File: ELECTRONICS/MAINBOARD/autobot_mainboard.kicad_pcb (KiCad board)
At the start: 4 copper layers, 50 x 38.5 mm, 162 parts, among them IC1 DW3210, J1 USB_C_Receptacle_USB2.0_16P, J10 Conn_01x05_Socket, J12 Conn_01x02_Pin, J17 Conn_01x02_Pin, J18 Conn_01x02_Pin, J19 Conn_02x05_Odd_Even, J20 Conn_02x05_Odd_Even, J4 Conn_01x02_Socket, J7 Conn_01x03_Pin, J8 Conn_Coaxial, J9 Conn_Coaxial, Q1 DMG1012T, Q2 DMG1012T, Q3 DMG1012T, Q4 DMG1012T, Q5 DMG1012T, SW1 RESET, SW2 BOOT, U1 TVS1400DRV, U10 VL53L1X, U11 VL53L1X, U12 VL53L1X, U13 BMI270, U14 BMI270, U16 LP5907MFX-3.3, U18 LP5907MFX-3.3, U19 STM32H743VITx, U2 LMR51430XDDCR, U23 LP5907MFX-3.3, U3 LP5907MFX-3.3, U4 TPD2EUSB30A, U7 STM32G031C_4-6-8_Tx, U8 TVS1400DRV, U9 VL53L1X, Y1 TXC 8Y38472012, Y2 25mhz placeholder

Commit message: functionally finished driver board
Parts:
- removed U8: TVS1400DRV, Package_SON:WSON-6-1EP_2x2mm_P0.65mm_EP1x1.6mm
- added C78: 100n, Capacitor_SMD:C_0402_1005Metric, F.Cu at (35.9, 31.2)
- added D13: PTVS17VZ1USK, Diode_SMD:Nexperia_CFP3_SOD-123W, F.Cu at (30.1, 53.9)
- added J11: Conn_01x01_Socket, Connector_Wire:SolderWire-0.25sqmm_1x01_D0.65mm_OD1.7mm, F.Cu at (60.4, 40.0)
- added J13: Conn_01x01_Socket, Connector_Wire:SolderWire-0.25sqmm_1x01_D0.65mm_OD1.7mm, F.Cu at (13.7, 34.1)
- added J2: Conn_01x01_Socket, Connector_Wire:SolderWire-0.25sqmm_1x01_D0.65mm_OD1.7mm, F.Cu at (60.4, 34.2)
- added J3: Conn_01x01_Socket, Connector_Wire:SolderWire-0.25sqmm_1x01_D0.65mm_OD1.7mm, F.Cu at (13.7, 39.9)
- added J5: Conn_01x01_Socket, Connector_Wire:SolderWire-0.25sqmm_1x01_D0.65mm_OD1.7mm, F.Cu at (60.4, 37.0)
- added J6: Conn_01x01_Socket, Connector_Wire:SolderWire-0.25sqmm_1x01_D0.65mm_OD1.7mm, F.Cu at (13.7, 37.0)
- added SW3: SW_Push, MyFootprintLibrary:SW-SMD_L3.9-W3.0-P4.45, F.Cu at (43.6, 20.1)
- SW1, SW2: footprint Button_Switch_THT:SW_PUSH_6mm -> MyFootprintLibrary:SW-SMD_L3.9-W3.0-P4.45
- moved SW1 56.8 mm to (283.6, 41.2)
- moved SW2 54.1 mm to (283.6, 45.5)
- moved U19 24.0 mm to (257.6, 57.2)
- moved C36 1.23 mm to (37.1, 29.8)
- moved C37 1.10 mm to (37.1, 28.9)
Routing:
- net /STM32G0/nRESET: track 0.00 -> 18.2 mm, vias 0 -> 2
- net GNDREF: track 48.1 -> 51.9 mm, vias 22 -> 26
- net +3V3: track 54.1 -> 56.1 mm
- net +24V: track 7.77 -> 9.68 mm
- net Net-(J3-Pin_1): track 6.92 -> 7.91 mm
- net Net-(J13-Pin_1): track 6.92 -> 7.87 mm
- net Net-(J11-Pin_1): track 7.05 -> 7.81 mm
- net Net-(J2-Pin_1): track 7.22 -> 7.81 mm

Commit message: driver done, unpolished
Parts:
- removed C1: 1u, Capacitor_SMD:C_0603_1608Metric
- removed C19, C21, C23, C25, C27, C28, C29, C30, C40, C45, C46, C47, C57, C60, C62, C63, C64, C65, C66, C67, C68, C69, C70, C71, C72: 100n, Capacitor_SMD:C_0402_1005Metric
- removed C2, C3: 100n, Capacitor_SMD:C_0603_1608Metric
- removed C20, C22, C24, C26, C49, C50: 10u, Capacitor_SMD:C_0402_1005Metric
- removed C34, C35, C5, C53, C54, C6, C61: 1u, Capacitor_SMD:C_0402_1005Metric
- removed C38, C39: 2p, Capacitor_SMD:C_0402_1005Metric
- removed C4: 47u, Capacitor_SMD:C_0603_1608Metric
- removed C41, C42, C43: 4.7n, Capacitor_SMD:C_0402_1005Metric
- removed C44: 220n, Capacitor_SMD:C_0402_1005Metric
- removed C48: 4.7u, Capacitor_SMD:C_0402_1005Metric
- removed C51, C52, C55, C56: 12p, Capacitor_SMD:C_0402_1005Metric
- removed C58, C59: 2.2u, Capacitor_SMD:C_0402_1005Metric
- removed C73: 4u7, Capacitor_SMD:C_0402_1005Metric
- removed D1: SS24, Diode_SMD:D_SMA
- removed D2, D3, D4: LED, LED_SMD:LED_0402_1005Metric
- removed FB2: fb, Resistor_SMD:R_0603_1608Metric
- removed FB3: FerriteBead_Small, Resistor_SMD:R_0402_1005Metric
- removed IC1: DW3210, MyFootprintLibrary:qfn_DW3220_QOR-M
- removed J1: USB_C_Receptacle_USB2.0_16P, Connector_USB:USB_C_Receptacle_GCT_USB4105-xx-A_16P_TopMnt_Horizontal
- removed J10: Conn_01x05_Socket, Connector_PinHeader_2.54mm:PinHeader_1x05_P2.54mm_Vertical
- removed J12: Conn_01x02_Pin, Connector_PinSocket_2.54mm:PinSocket_1x02_P2.54mm_Vertical
- removed J19: Conn_02x05_Odd_Even, Connector_PinSocket_2.54mm:PinSocket_2x05_P2.54mm_Vertical
- removed J7: Conn_01x03_Pin, Connector_PinHeader_2.54mm:PinHeader_1x03_P2.54mm_Vertical
- removed J8, J9: Conn_Coaxial, Connector_Coaxial:U.FL_Hirose_U.FL-R-SMT-1_Vertical
- removed L1: 5.6u, Inductor_SMD:L_APV_APH0840
- removed Q1, Q2, Q3: DMG1012T, Package_TO_SOT_SMD:SOT-523
- removed R1: 162k, Resistor_SMD:R_0603_1608Metric
- removed R15, R16, R21: 10k, Resistor_SMD:R_0402_1005Metric
- removed R17: 100K, Resistor_SMD:R_0402_1005Metric
- removed R18, R19, R20: R, Resistor_SMD:R_0402_1005Metric
- removed R2: 22.1k, Resistor_SMD:R_0603_1608Metric
- removed R22: 47, Resistor_SMD:R_0402_1005Metric_Pad0.72x0.64mm_HandSolder
- removed R3, R4: 5.1k, Resistor_SMD:R_0402_1005Metric
- removed R5, R6: 22, Resistor_SMD:R_0402_1005Metric
- removed SW1: RESET, MyFootprintLibrary:SW-SMD_L3.9-W3.0-P4.45
- removed SW2: BOOT, MyFootprintLibrary:SW-SMD_L3.9-W3.0-P4.45
- removed U1: TVS1400DRV, Package_SON:WSON-6-1EP_2x2mm_P0.65mm_EP1x1.6mm
- removed U10, U11, U12, U9: VL53L1X, Connector_JST:JST_PH_S6B-PH-K_1x06_P2.00mm_Horizontal
- removed U13, U14: BMI270, MyFootprintLibrary:BMI270_BOS-M
- removed U16, U18, U3: LP5907MFX-3.3, Package_TO_SOT_SMD:SOT-23-5
- removed U19: STM32H743VITx, Package_QFP:LQFP-100_14x14mm_P0.5mm
- removed U2: LMR51430XDDCR, MyFootprintLibrary:SOT-23-THIN-6_DDC_TEX
- removed U4: TPD2EUSB30A, Package_TO_SOT_SMD:Texas_DRT-3
- removed Y1: TXC 8Y38472012, Crystal:Crystal_SMD_2016-4Pin_2.0x1.6mm
- removed Y2: 25mhz placeholder, Crystal:Crystal_SMD_2016-4Pin_2.0x1.6mm
- U5, U6: footprint MyFootprintLibrary:VQFN-40_L7.0-W5.0-P0.50-BL-EP5.7 -> MyFootprintLibrary:VQFN40_RGF_TEX_mct8316
- moved C12 0.23 mm to (45.5, 40.5)
- moved C74 0.23 mm to (28.6, 33.5)
- turned U5 to 90 degrees
- turned U6 to -90 degrees
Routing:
- net +5V: track 81.4 -> 71.2 mm
- net GNDREF: track 51.9 -> 41.7 mm, vias 26 -> 29
- net /STM32G0/nRESET: track 18.2 -> 17.7 mm

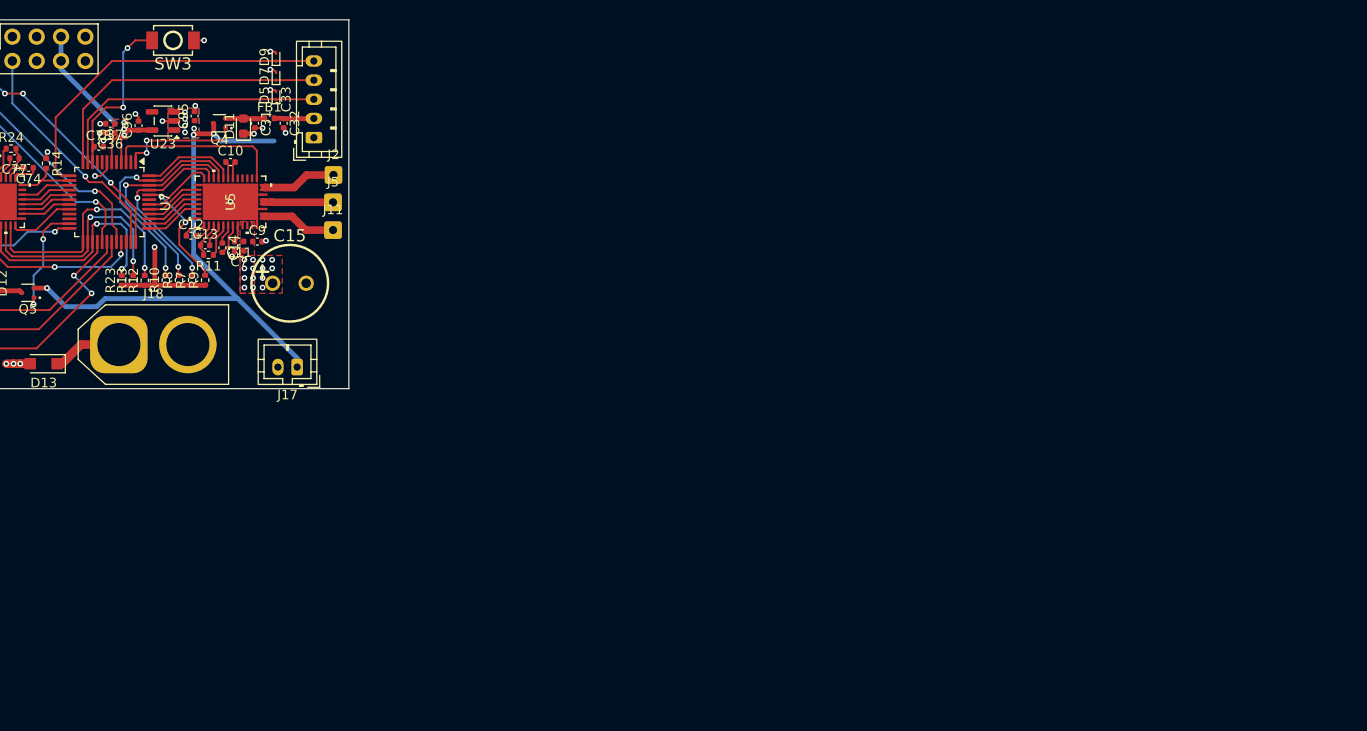
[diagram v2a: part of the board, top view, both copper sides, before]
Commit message: edit boost converter, added gnd planes, polish later
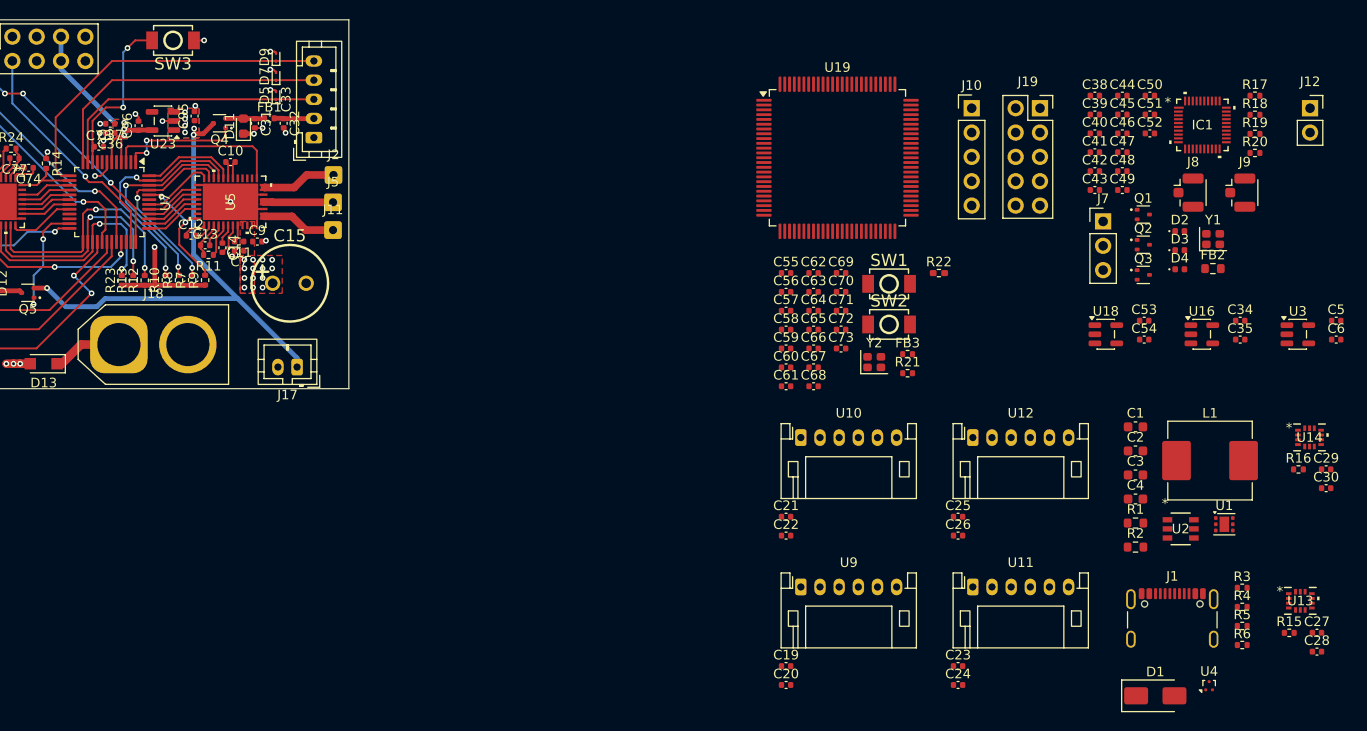
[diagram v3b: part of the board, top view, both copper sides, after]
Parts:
- added C1: 1u, Capacitor_SMD:C_0603_1608Metric, F.Cu at (144.1, 60.5)
- added C19: 100n, Capacitor_SMD:C_0402_1005Metric, F.Cu at (107.6, 85.5)
- added C2: 100n, Capacitor_SMD:C_0603_1608Metric, F.Cu at (144.1, 63.0)
- added C20: 10u, Capacitor_SMD:C_0402_1005Metric, F.Cu at (107.6, 87.4)
- added C21: 100n, Capacitor_SMD:C_0402_1005Metric, F.Cu at (107.6, 69.9)
- added C22: 10u, Capacitor_SMD:C_0402_1005Metric, F.Cu at (107.6, 71.8)
- added C23: 100n, Capacitor_SMD:C_0402_1005Metric, F.Cu at (125.6, 85.5)
- added C24: 10u, Capacitor_SMD:C_0402_1005Metric, F.Cu at (125.6, 87.4)
- added C25: 100n, Capacitor_SMD:C_0402_1005Metric, F.Cu at (125.6, 69.9)
- added C26: 10u, Capacitor_SMD:C_0402_1005Metric, F.Cu at (125.6, 71.8)
- added C27: 100n, Capacitor_SMD:C_0402_1005Metric, F.Cu at (163.1, 82.0)
- added C28: 100n, Capacitor_SMD:C_0402_1005Metric, F.Cu at (163.1, 84.0)
- added C29: 100n, Capacitor_SMD:C_0402_1005Metric, F.Cu at (164.0, 64.9)
- added C3: 100n, Capacitor_SMD:C_0603_1608Metric, F.Cu at (144.1, 65.5)
- added C30: 100n, Capacitor_SMD:C_0402_1005Metric, F.Cu at (164.0, 66.9)
- added C34: 1u, Capacitor_SMD:C_0402_1005Metric, F.Cu at (155.0, 49.4)
- added C35: 1u, Capacitor_SMD:C_0402_1005Metric, F.Cu at (155.0, 51.4)
- added C38: 2p, Capacitor_SMD:C_0402_1005Metric, F.Cu at (139.9, 25.9)
- added C39: 2p, Capacitor_SMD:C_0402_1005Metric, F.Cu at (139.9, 27.9)
- added C4: 47u, Capacitor_SMD:C_0603_1608Metric, F.Cu at (144.1, 68.0)
- added C40: 100n, Capacitor_SMD:C_0402_1005Metric, F.Cu at (139.9, 29.9)
- added C41: 4.7n, Capacitor_SMD:C_0402_1005Metric, F.Cu at (139.9, 31.8)
- added C42: 4.7n, Capacitor_SMD:C_0402_1005Metric, F.Cu at (139.9, 33.8)
- added C43: 4.7n, Capacitor_SMD:C_0402_1005Metric, F.Cu at (139.9, 35.8)
- added C44: 220n, Capacitor_SMD:C_0402_1005Metric, F.Cu at (142.7, 25.9)
- added C45: 100n, Capacitor_SMD:C_0402_1005Metric, F.Cu at (142.7, 27.9)
- added C46: 100n, Capacitor_SMD:C_0402_1005Metric, F.Cu at (142.7, 29.9)
- added C47: 100n, Capacitor_SMD:C_0402_1005Metric, F.Cu at (142.7, 31.8)
- added C48: 4.7u, Capacitor_SMD:C_0402_1005Metric, F.Cu at (142.7, 33.8)
- added C49: 10u, Capacitor_SMD:C_0402_1005Metric, F.Cu at (142.7, 35.8)
- added C5: 1u, Capacitor_SMD:C_0402_1005Metric, F.Cu at (165.1, 49.4)
- added C50: 10u, Capacitor_SMD:C_0402_1005Metric, F.Cu at (145.6, 25.9)
- added C51: 12p, Capacitor_SMD:C_0402_1005Metric, F.Cu at (145.6, 27.9)
- added C52: 12p, Capacitor_SMD:C_0402_1005Metric, F.Cu at (145.6, 29.9)
- added C53: 1u, Capacitor_SMD:C_0402_1005Metric, F.Cu at (145.0, 49.4)
- added C54: 1u, Capacitor_SMD:C_0402_1005Metric, F.Cu at (145.0, 51.4)
- added C55: 12p, Capacitor_SMD:C_0402_1005Metric, F.Cu at (107.6, 44.4)
- added C56: 12p, Capacitor_SMD:C_0402_1005Metric, F.Cu at (107.6, 46.4)
- added C57: 100n, Capacitor_SMD:C_0402_1005Metric, F.Cu at (107.6, 48.4)
- added C58: 2.2u, Capacitor_SMD:C_0402_1005Metric, F.Cu at (107.6, 50.3)
- added C59: 2.2u, Capacitor_SMD:C_0402_1005Metric, F.Cu at (107.6, 52.3)
- added C6: 1u, Capacitor_SMD:C_0402_1005Metric, F.Cu at (165.1, 51.4)
- added C60: 100n, Capacitor_SMD:C_0402_1005Metric, F.Cu at (107.6, 54.3)
- added C61: 1u, Capacitor_SMD:C_0402_1005Metric, F.Cu at (107.6, 56.2)
- added C62: 100n, Capacitor_SMD:C_0402_1005Metric, F.Cu at (110.5, 44.4)
- added C63: 100n, Capacitor_SMD:C_0402_1005Metric, F.Cu at (110.5, 46.4)
- added C64: 100n, Capacitor_SMD:C_0402_1005Metric, F.Cu at (110.5, 48.4)
- added C65: 100n, Capacitor_SMD:C_0402_1005Metric, F.Cu at (110.5, 50.3)
- added C66: 100n, Capacitor_SMD:C_0402_1005Metric, F.Cu at (110.5, 52.3)
- added C67: 100n, Capacitor_SMD:C_0402_1005Metric, F.Cu at (110.5, 54.3)
- added C68: 100n, Capacitor_SMD:C_0402_1005Metric, F.Cu at (110.5, 56.2)
- added C69: 100n, Capacitor_SMD:C_0402_1005Metric, F.Cu at (113.4, 44.4)
- added C70: 100n, Capacitor_SMD:C_0402_1005Metric, F.Cu at (113.4, 46.4)
- added C71: 100n, Capacitor_SMD:C_0402_1005Metric, F.Cu at (113.4, 48.4)
- added C72: 100n, Capacitor_SMD:C_0402_1005Metric, F.Cu at (113.4, 50.3)
- added C73: 4u7, Capacitor_SMD:C_0402_1005Metric, F.Cu at (113.4, 52.3)
- added D1: SS24, Diode_SMD:D_SMA, F.Cu at (146.2, 88.6)
- added D2: LED, LED_SMD:LED_0402_1005Metric, F.Cu at (148.7, 40.1)
- added D3: LED, LED_SMD:LED_0402_1005Metric, F.Cu at (148.7, 42.0)
- added D4: LED, LED_SMD:LED_0402_1005Metric, F.Cu at (148.7, 44.0)
- added FB2: fb, Resistor_SMD:R_0603_1608Metric, F.Cu at (152.2, 44.0)
- added FB3: FerriteBead_Small, Resistor_SMD:R_0402_1005Metric, F.Cu at (120.3, 52.9)
- added IC1: DW3210, MyFootprintLibrary:qfn_DW3220_QOR-M, F.Cu at (151.1, 29.0)
- added J1: USB_C_Receptacle_USB2.0_16P, Connector_USB:USB_C_Receptacle_GCT_USB4105-xx-A_16P_TopMnt_Horizontal, F.Cu at (147.9, 81.6)
- added J10: Conn_01x05_Socket, Connector_PinHeader_2.54mm:PinHeader_1x05_P2.54mm_Vertical, F.Cu at (127.0, 27.2)
- added J12: Conn_01x02_Pin, Connector_PinSocket_2.54mm:PinSocket_1x02_P2.54mm_Vertical, F.Cu at (162.3, 27.2)
- added J19: Conn_02x05_Odd_Even, Connector_PinSocket_2.54mm:PinSocket_2x05_P2.54mm_Vertical, F.Cu at (134.1, 27.2)
- added J7: Conn_01x03_Pin, Connector_PinHeader_2.54mm:PinHeader_1x03_P2.54mm_Vertical, F.Cu at (140.7, 39.0)
- added J8: Conn_Coaxial, Connector_Coaxial:U.FL_Hirose_U.FL-R-SMT-1_Vertical, F.Cu at (150.1, 36.0)
- added J9: Conn_Coaxial, Connector_Coaxial:U.FL_Hirose_U.FL-R-SMT-1_Vertical, F.Cu at (155.5, 36.0)
- added L1: 5.6u, Inductor_SMD:L_APV_APH0840, F.Cu at (151.9, 64.0)
- added Q1: DMG1012T, Package_TO_SOT_SMD:SOT-523, F.Cu at (144.9, 38.3)
- added Q2: DMG1012T, Package_TO_SOT_SMD:SOT-523, F.Cu at (144.9, 41.5)
- added Q3: DMG1012T, Package_TO_SOT_SMD:SOT-523, F.Cu at (144.9, 44.6)
- added R1: 162k, Resistor_SMD:R_0603_1608Metric, F.Cu at (144.1, 70.5)
- added R15: 10k, Resistor_SMD:R_0402_1005Metric, F.Cu at (160.2, 82.0)
- added R16: 10k, Resistor_SMD:R_0402_1005Metric, F.Cu at (161.1, 64.9)
- added R17: 100K, Resistor_SMD:R_0402_1005Metric, F.Cu at (156.6, 25.9)
- added R18: R, Resistor_SMD:R_0402_1005Metric, F.Cu at (156.6, 27.9)
- added R19: R, Resistor_SMD:R_0402_1005Metric, F.Cu at (156.6, 29.9)
- added R2: 22.1k, Resistor_SMD:R_0603_1608Metric, F.Cu at (144.1, 73.0)
- added R20: R, Resistor_SMD:R_0402_1005Metric, F.Cu at (156.6, 31.9)
- added R21: 10k, Resistor_SMD:R_0402_1005Metric, F.Cu at (120.3, 54.9)
- added R22: 47, Resistor_SMD:R_0402_1005Metric_Pad0.72x0.64mm_HandSolder, F.Cu at (123.6, 44.4)
- added R3: 5.1k, Resistor_SMD:R_0402_1005Metric, F.Cu at (155.2, 77.3)
- added R4: 5.1k, Resistor_SMD:R_0402_1005Metric, F.Cu at (155.2, 79.3)
- added R5: 22, Resistor_SMD:R_0402_1005Metric, F.Cu at (155.2, 81.3)
- added R6: 22, Resistor_SMD:R_0402_1005Metric, F.Cu at (155.2, 83.3)
- added SW1: RESET, MyFootprintLibrary:SW-SMD_L3.9-W3.0-P4.45, F.Cu at (118.4, 45.6)
- added SW2: BOOT, MyFootprintLibrary:SW-SMD_L3.9-W3.0-P4.45, F.Cu at (118.4, 49.8)
- added U1: TVS1400DRV, Package_SON:WSON-6-1EP_2x2mm_P0.65mm_EP1x1.6mm, F.Cu at (153.4, 70.7)
- added U10: VL53L1X, Connector_JST:JST_PH_S6B-PH-K_1x06_P2.00mm_Horizontal, F.Cu at (109.2, 61.6)
- added U11: VL53L1X, Connector_JST:JST_PH_S6B-PH-K_1x06_P2.00mm_Horizontal, F.Cu at (127.1, 77.2)
- added U12: VL53L1X, Connector_JST:JST_PH_S6B-PH-K_1x06_P2.00mm_Horizontal, F.Cu at (127.1, 61.6)
- added U13: BMI270, MyFootprintLibrary:BMI270_BOS-M, F.Cu at (161.3, 78.6)
- added U14: BMI270, MyFootprintLibrary:BMI270_BOS-M, F.Cu at (162.3, 61.6)
- added U16: LP5907MFX-3.3, Package_TO_SOT_SMD:SOT-23-5, F.Cu at (151.0, 50.8)
- added U18: LP5907MFX-3.3, Package_TO_SOT_SMD:SOT-23-5, F.Cu at (141.0, 50.8)
- added U19: STM32H743VITx, Package_QFP:LQFP-100_14x14mm_P0.5mm, F.Cu at (113.0, 32.4)
- added U2: LMR51430XDDCR, MyFootprintLibrary:SOT-23-THIN-6_DDC_TEX, F.Cu at (148.8, 71.1)
- added U3: LP5907MFX-3.3, Package_TO_SOT_SMD:SOT-23-5, F.Cu at (161.1, 50.8)
- added U4: TPD2EUSB30A, Package_TO_SOT_SMD:Texas_DRT-3, F.Cu at (151.8, 87.5)
- added U9: VL53L1X, Connector_JST:JST_PH_S6B-PH-K_1x06_P2.00mm_Horizontal, F.Cu at (109.2, 77.2)
- added Y1: TXC 8Y38472012, Crystal:Crystal_SMD_2016-4Pin_2.0x1.6mm, F.Cu at (152.2, 40.9)
- added Y2: 25mhz placeholder, Crystal:Crystal_SMD_2016-4Pin_2.0x1.6mm, F.Cu at (116.8, 53.7)
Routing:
- net +5V: track 71.2 -> 63.9 mm, vias 8 -> 7
- net +24V: track 9.68 -> 7.77 mm
- net Net-(U5-CP): track 2.28 -> 1.78 mm

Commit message: port dw3220 routing to mainboard; copy shit
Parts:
- moved U19 126.3 mm to (230.0, 80.0)
- moved J7 107.5 mm to (247.7, 49.8), turned to 180 degrees
- moved Q3 97.9 mm to (242.6, 52.2), turned to -90 degrees
- moved D4 94.8 mm to (242.6, 57.5), turned to -90 degrees
- moved Q2 94.7 mm to (239.1, 52.2), turned to -90 degrees
- moved C40 93.4 mm to (231.1, 50.0), turned to -90 degrees
- moved Q1 91.7 mm to (235.6, 52.2), turned to -90 degrees
- moved C39 91.6 mm to (230.6, 41.1), turned to -90 degrees
- moved D3 91.6 mm to (239.1, 57.5), turned to -90 degrees
- moved C38 90.0 mm to (228.6, 41.1), turned to -90 degrees
- moved R20 88.9 mm to (242.6, 54.5), turned to 90 degrees
- moved D2 88.5 mm to (235.6, 57.5), turned to -90 degrees
- moved R19 86.1 mm to (239.1, 54.5), turned to 90 degrees
- moved C41 85.5 mm to (223.3, 50.7), turned to 180 degrees
- moved C45 85.5 mm to (225.5, 49.6)
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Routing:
- net (no net): track 0.00 -> 29.4 mm, vias 0 -> 4
- net +3V3: track 56.0 -> 82.6 mm, vias 5 -> 20
- net /DW3220_T/DW_GPIO0: track 0.00 -> 17.0 mm
- net /DW3220_T/DW_GPIO4: track 0.00 -> 16.7 mm
- net /DW3220_T/DW_GPIO7: track 0.00 -> 15.8 mm
- net GNDREF: track 41.6 -> 55.2 mm, vias 29 -> 59
- net /DW3220_T/RX_OK_LED: track 0.00 -> 8.73 mm, vias 0 -> 2
- net Net-(IC1-VDD2A): track 0.00 -> 5.99 mm
- net /DW3220_T/XTO: track 0.00 -> 5.56 mm
- net /DW3220_T/CSN: track 0.00 -> 5.09 mm
- net /DW3220_T/XTI: track 0.00 -> 4.97 mm
- net Net-(IC1-VTX_D): track 0.00 -> 4.04 mm
- net Net-(D3-K): track 0.00 -> 2.01 mm
- net Net-(D2-K): track 0.00 -> 2.01 mm
- net Net-(D4-K): track 0.00 -> 2.00 mm
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- added copper zone on F.Cu, net GNDREF
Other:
- board text added: "maybe use 0201"

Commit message: update
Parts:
- moved C23 173.5 mm to (298.4, 101.9)
- moved R15 173.5 mm to (332.9, 98.5)
- moved R22 173.5 mm to (296.4, 60.9)
- moved U14 173.5 mm to (335.0, 78.1)
- moved Y2 173.5 mm to (289.6, 70.2)
- moved C1 173.5 mm to (316.9, 77.0)
- moved C19 173.5 mm to (280.4, 101.9)
- moved C2 173.5 mm to (316.9, 79.5)
- moved C24 173.5 mm to (298.4, 103.9)
- moved C25 173.5 mm to (298.4, 86.3)
- moved C26 173.5 mm to (298.4, 88.3)
- moved C28 173.5 mm to (335.8, 100.4)
- moved C29 173.5 mm to (336.8, 81.4)
- moved C30 173.5 mm to (336.8, 83.4)
- moved C4 173.5 mm to (316.9, 84.5)
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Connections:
- U19 pad 10: Net-(U19-VSS-Pad10) -> GNDREF
- U19 pad 19: unconnected-(U19-VSSA-Pad19) -> GNDREF
- U19 pad 26: Net-(U19-VSS-Pad10) -> GNDREF
- U19 pad 49: Net-(U19-VSS-Pad10) -> GNDREF
- U19 pad 74: Net-(U19-VSS-Pad10) -> GNDREF
- U19 pad 95: /STM32H743/DIR_L -> unconnected-(U19-PB8-Pad95)
- U19 pad 96: /STM32H743/STEP_L -> unconnected-(U19-PB9-Pad96)
- U19 pad 99: Net-(U19-VSS-Pad10) -> GNDREF
